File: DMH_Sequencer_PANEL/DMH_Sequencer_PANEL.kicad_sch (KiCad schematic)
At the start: 53 parts, among them J0 Panel_GND_Solder_Wire_Pad

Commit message: Main controls position test ongoing
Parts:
- added H1: LED Step 1, SynthStuff:MountingHole_LED_3mm_R, symbol Mechanical:MountingHole
- added H1003, H1004, H1007, H1008: MountingHole_Rails, SynthStuff:MountingHole_Rails, symbol SynthStuff:MountingHole_Rails
- added H2: LED Step 2, SynthStuff:MountingHole_LED_3mm_R, symbol Mechanical:MountingHole
- added H3: LED Step 3, SynthStuff:MountingHole_LED_3mm_R, symbol Mechanical:MountingHole
- added H33: LED Step 9, SynthStuff:MountingHole_LED_3mm_R, symbol Mechanical:MountingHole
- added H34: LED Step 10, SynthStuff:MountingHole_LED_3mm_R, symbol Mechanical:MountingHole
- added H35: LED Step 11, SynthStuff:MountingHole_LED_3mm_R, symbol Mechanical:MountingHole
- added H36: LED Step 12, SynthStuff:MountingHole_LED_3mm_R, symbol Mechanical:MountingHole
- added H37: LED Step 13, SynthStuff:MountingHole_LED_3mm_R, symbol Mechanical:MountingHole
- added H38: LED Step 14, SynthStuff:MountingHole_LED_3mm_R, symbol Mechanical:MountingHole
- added H39: LED Step 15, SynthStuff:MountingHole_LED_3mm_R, symbol Mechanical:MountingHole
- added H4: LED Step 4, SynthStuff:MountingHole_LED_3mm_R, symbol Mechanical:MountingHole
- added H40: LED Step 16, SynthStuff:MountingHole_LED_3mm_R, symbol Mechanical:MountingHole
- added H5: LED Step 5, SynthStuff:MountingHole_LED_3mm_R, symbol Mechanical:MountingHole
- added H6: LED Step 6, SynthStuff:MountingHole_LED_3mm_R, symbol Mechanical:MountingHole
- added H65: Gate Out 1, SynthStuff:Jack_6.35mm_Cutout_Output_v6, symbol SynthStuff:MountingHole_Jack6.35mm_Output_v2
- added H66: Gate Out 2, SynthStuff:Jack_6.35mm_Cutout_Output_v6, symbol SynthStuff:MountingHole_Jack6.35mm_Output_v2
- added H67: Gate Out 3, SynthStuff:Jack_6.35mm_Cutout_Output_v6, symbol SynthStuff:MountingHole_Jack6.35mm_Output_v2
- added H68: Gate Out 4, SynthStuff:Jack_6.35mm_Cutout_Output_v6, symbol SynthStuff:MountingHole_Jack6.35mm_Output_v2
- added H69: Gate Out 5, SynthStuff:Jack_6.35mm_Cutout_Output_v6, symbol SynthStuff:MountingHole_Jack6.35mm_Output_v2
- added H7: LED Step 7, SynthStuff:MountingHole_LED_3mm_R, symbol Mechanical:MountingHole
- added H70: Gate Out 6, SynthStuff:Jack_6.35mm_Cutout_Output_v6, symbol SynthStuff:MountingHole_Jack6.35mm_Output_v2
- added H71: Gate Out 7, SynthStuff:Jack_6.35mm_Cutout_Output_v6, symbol SynthStuff:MountingHole_Jack6.35mm_Output_v2
- added H72: Gate Out 8, SynthStuff:Jack_6.35mm_Cutout_Output_v6, symbol SynthStuff:MountingHole_Jack6.35mm_Output_v2
- added H8: LED Step 8, SynthStuff:MountingHole_LED_3mm_R, symbol Mechanical:MountingHole
- H17: renamed from H13; value Gate Length 1 -> GL 1
- H18: renamed from H14; value Gate Length 2 -> GL 2
- H19: renamed from H15; value Gate Length 3 -> GL 3
- H20: renamed from H16; value Gate Length 4 -> GL 4
- H21: renamed from H17; value Gate Length 5 -> GL 5
- H22: renamed from H18; value Gate Length 6 -> GL 6
- H23: renamed from H19; value Gate Length 7 -> GL 7
- H24: renamed from H20; value Gate Length 8 -> GL 8
- H49: renamed from H29; value Gate Length 9 -> GL 9
- H50: renamed from H30; value Gate Length 10 -> GL 10
- H51: renamed from H31; value Gate Length 11 -> GL 11
- H52: renamed from H32; value Gate Length 12 -> GL 12
- H53: renamed from H33; value Gate Length 13 -> GL 13
- H54: renamed from H34; value Gate Length 14 -> GL 14
- H55: renamed from H35; value Gate Length 15 -> GL 15
- H56: renamed from H36; value Gate Length 16 -> GL 16
- renumbered H6 to H10, H1 to H1001, H2 to H1002, H3 to H1005, H4 to H1006, H7 to H11, H8 to H12, H9 to H13, H10 to H14, H11 to H15, H12 to H16, H37 to H25, H38 to H26, H39 to H27, H40 to H28, H41 to H29, H42 to H30, H43 to H31, H44 to H32, H21 to H41, H22 to H42, H23 to H43, H24 to H44, H25 to H45, H26 to H46, H27 to H47, H28 to H48, H45 to H57, H46 to H58, H47 to H59, H48 to H60, H49 to H61, H50 to H62, H51 to H63, H52 to H64, H5 to H9
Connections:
- net GND: now also H1003.1, H1004.1, H1007.1, H1008.1
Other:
- moved on the sheet: H10, H1002, H1006, H11, H12, H13, H14, H15, H16, H17, H18, H19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

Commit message: First Layout ready
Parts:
- added H73: Clock, SynthStuff:Pot_Cutout_Medium_v2, symbol SynthStuff:MountingHole_Pot
- added H74: Clk CV Amt, SynthStuff:Pot_Cutout_Tiny_attv_P110KH1, symbol SynthStuff:MountingHole_Pot
- added H75: Transp, SynthStuff:Pot_Cutout_Tiny, symbol SynthStuff:MountingHole_Pot
- added H76: Transp CV Amt, SynthStuff:Pot_Cutout_Tiny_attv_P110KH1, symbol SynthStuff:MountingHole_Pot
- added H77: Slew, SynthStuff:Pot_Cutout_Tiny, symbol SynthStuff:MountingHole_Pot
- added H78: Slew CV Amt, SynthStuff:Pot_Cutout_Tiny_attv_P110KH1, symbol SynthStuff:MountingHole_Pot
- added H79: Direction, SynthStuff:Selector_Cutout_5pos, symbol SynthStuff:MountingHole_Pot
- added H80: Mode, SynthStuff:Toggle_Switch_TE_Cutout, symbol SynthStuff:MountingHole_ToggleSwitch
- added H81: Clock, SynthStuff:Toggle_Switch_TE_Cutout, symbol SynthStuff:MountingHole_ToggleSwitch
- added H82: Quant, SynthStuff:Toggle_Switch_TE_Cutout, symbol SynthStuff:MountingHole_ToggleSwitch
- added H83: Step, SynthStuff:MX_switch_Cutout, symbol Mechanical:MountingHole
- added H84: Reset, SynthStuff:MX_switch_Cutout, symbol Mechanical:MountingHole
- added H85: LED Quant, SynthStuff:MountingHole_LED_3mm_R, symbol Mechanical:MountingHole
- added H86: CV 1-8, SynthStuff:Jack_6.35mm_Cutout_Output_v6, symbol SynthStuff:MountingHole_Jack6.35mm_Output_v2
- added H87: CV 9-16, SynthStuff:Jack_6.35mm_Cutout_Output_v6, symbol SynthStuff:MountingHole_Jack6.35mm_Output_v2
- added H88: Gate, SynthStuff:Jack_6.35mm_Cutout_Output_v6, symbol SynthStuff:MountingHole_Jack6.35mm_Output_v2
- added H89: Gate 9-16, SynthStuff:Jack_6.35mm_Cutout_Output_v6, symbol SynthStuff:MountingHole_Jack6.35mm_Output_v2
- added H90: Clock, SynthStuff:Jack_6.35mm_Cutout_v3, symbol SynthStuff:MountingHole_Jack6.35mm_v2
- added H91: Reset, SynthStuff:Jack_6.35mm_Cutout_v3, symbol SynthStuff:MountingHole_Jack6.35mm_v2
- added H92: Transp, SynthStuff:Jack_6.35mm_Cutout_v3, symbol SynthStuff:MountingHole_Jack6.35mm_v2
- H65, H66, H67, H68, H69, H70, H71, H72: now not fitted

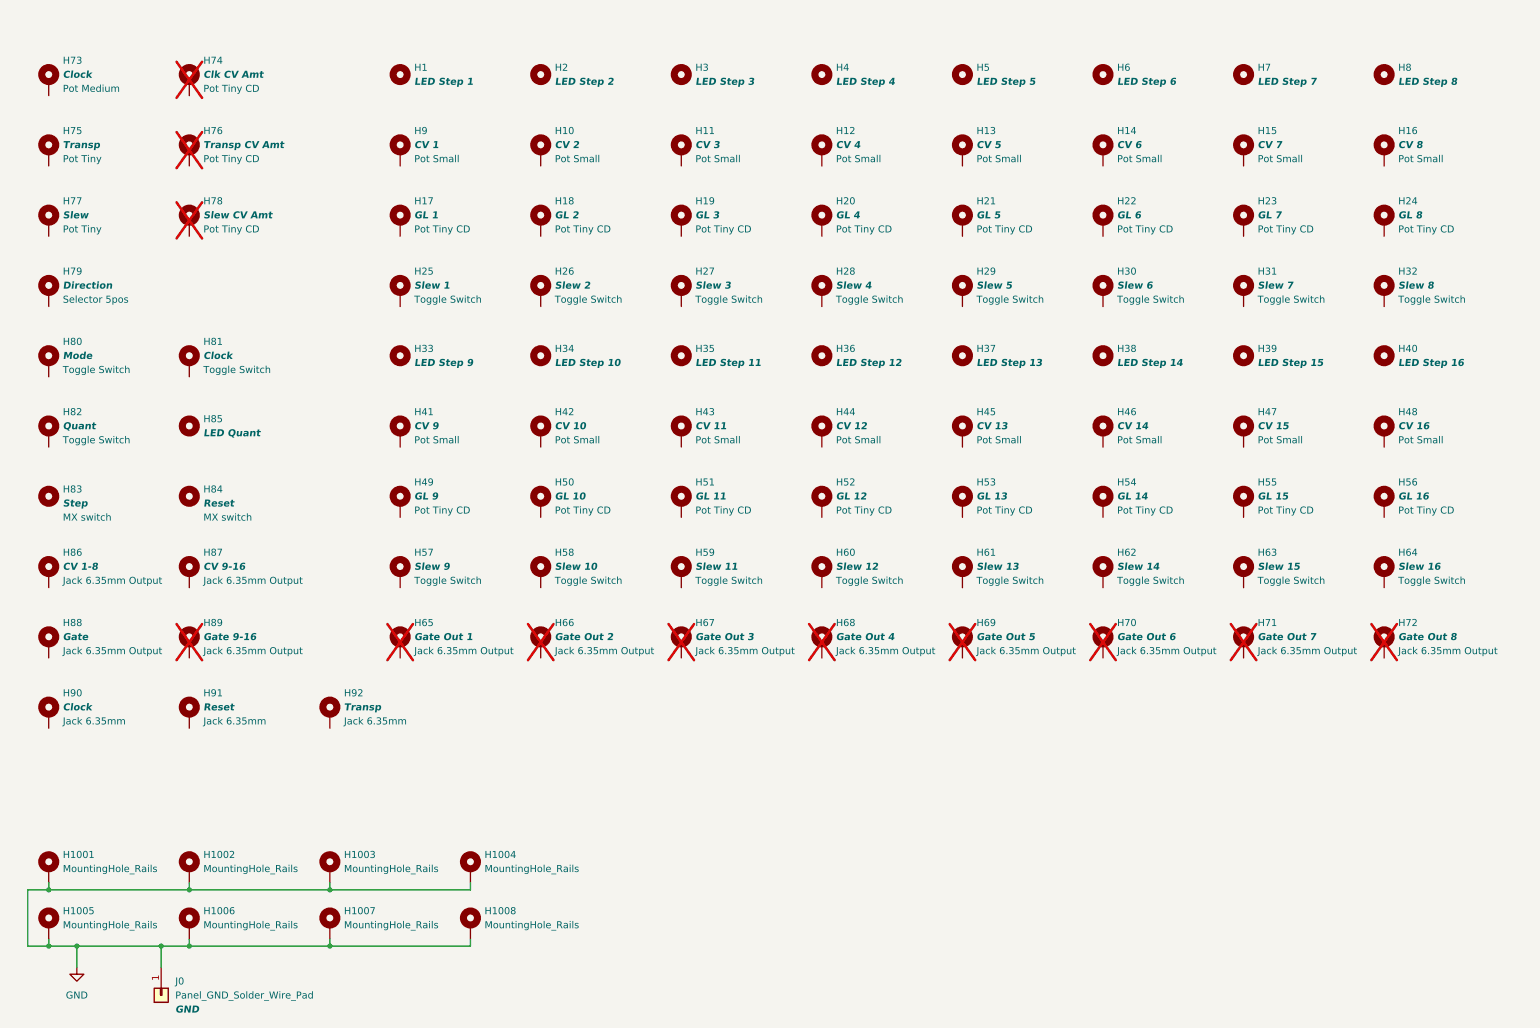
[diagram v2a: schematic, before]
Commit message: Updated selector 3D model
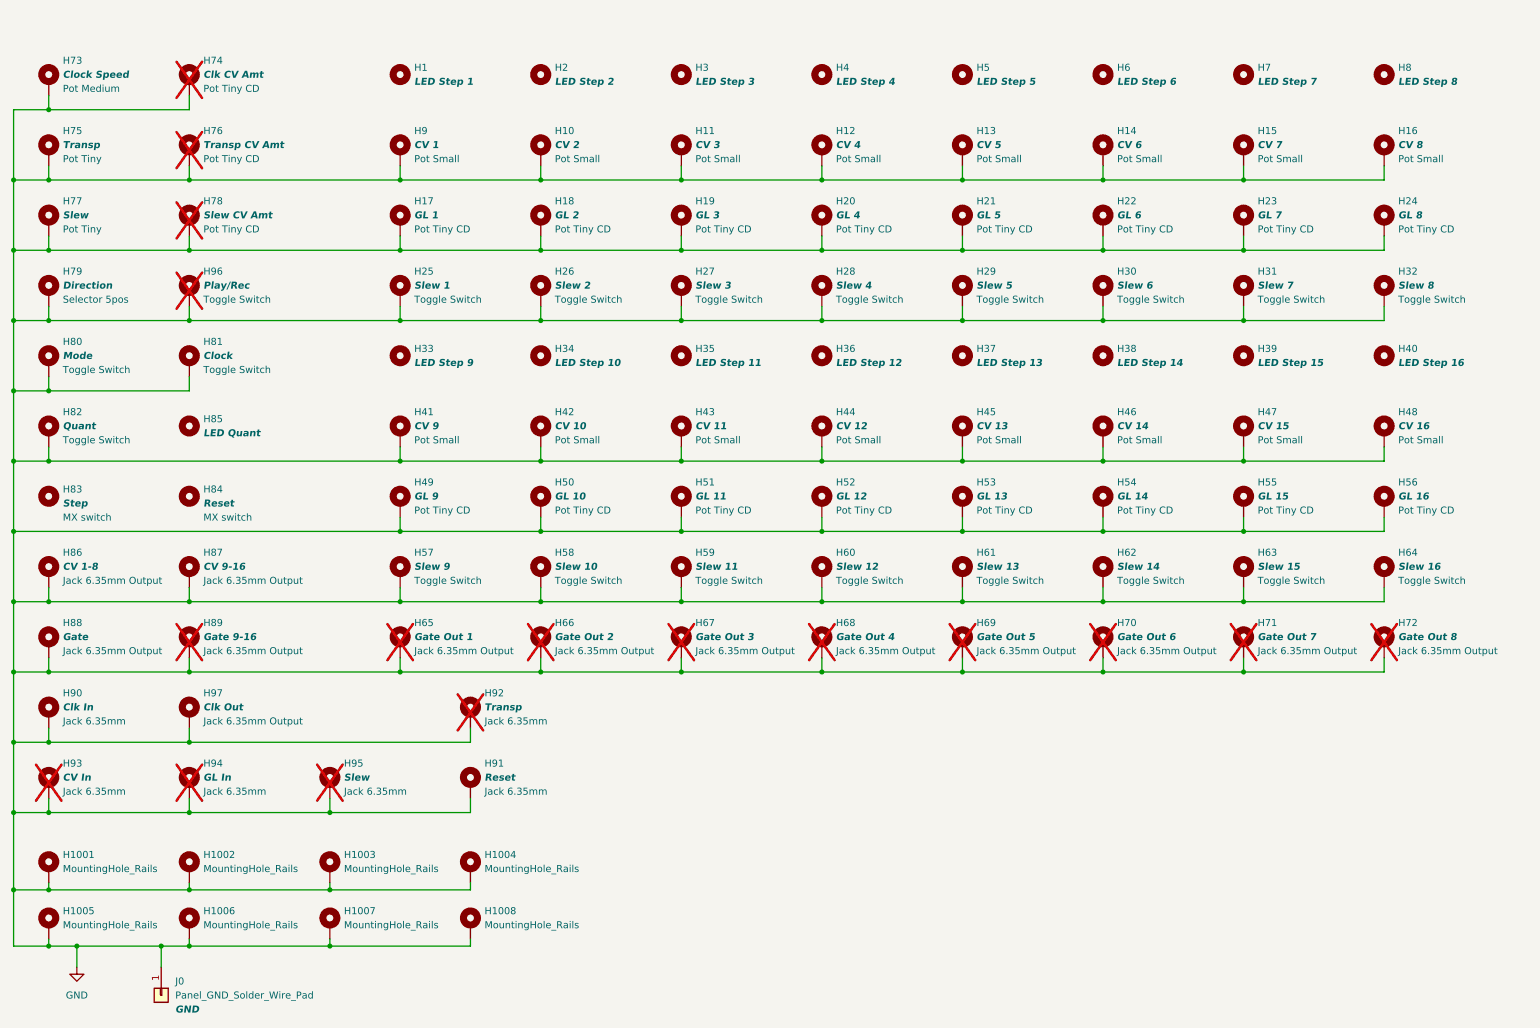
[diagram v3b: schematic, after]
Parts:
- added H93: CV In, SynthStuff:Jack_6.35mm_Cutout_v3, symbol SynthStuff:MountingHole_Jack6.35mm_v2
- added H94: GL In, SynthStuff:Jack_6.35mm_Cutout_v3, symbol SynthStuff:MountingHole_Jack6.35mm_v2
- added H95: Slew, SynthStuff:Jack_6.35mm_Cutout_v3, symbol SynthStuff:MountingHole_Jack6.35mm_v2
- added H96: Play/Rec, SynthStuff:Toggle_Switch_TE_Cutout, symbol SynthStuff:MountingHole_ToggleSwitch
- added H97: Clk Out, SynthStuff:Jack_6.35mm_Cutout_Output_v6, symbol SynthStuff:MountingHole_Jack6.35mm_Output_v2
- H73: value Clock -> Clock Speed
- H85: footprint SynthStuff:MountingHole_LED_3mm_R -> SynthStuff:MountingHole_LED_3mm_B
- H90: value Clock -> Clk In
- H92: now not fitted
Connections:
- net GND: now also H10.1, H11.1, H12.1, H13.1, H14.1, H15.1, H16.1, H17.1, H18.1, H19.1, H20.1, H21.1, H22.1, H23.1, H24.1, H25.1, H26.1, H27.1, H28.1, H29.1, H30.1, H31.1, H32.1, H41.1, H42.1, H43.1, H44.1, H45.1, H46.1, H47.1, H48.1, H49.1, H50.1, H51.1, H52.1, H53.1, H54.1, H55.1, H56.1, H57.1, H58.1, H59.1, H60.1, H61.1, H62.1, H63.1, H64.1, H65.1, H66.1, H67.1, H68.1, H69.1, H70.1, H71.1, H72.1, H73.1, H74.1, H75.1, H76.1, H77.1, H78.1, H79.1, H80.1, H81.1, H82.1, H86.1, H87.1, H88.1, H89.1, H9.1, H90.1, H91.1, H92.1, H93.1, H94.1, H95.1, H96.1, H97.1
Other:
- moved on the sheet: H91

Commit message: Added clock PPQN selector
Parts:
- added H98: LED Clock, SynthStuff:MountingHole_LED_3mm_R, symbol Mechanical:MountingHole
- added H99: Clk PPQN, SynthStuff:Selector_Cutout_SRBV151102, symbol SynthStuff:MountingHole_Selector
- H75: footprint SynthStuff:Pot_Cutout_Tiny -> SynthStuff:Pot_Cutout_Tiny_attv_RD901F
- H79: footprint SynthStuff:Selector_Cutout_5pos -> SynthStuff:Selector_Cutout_SRBV151102; symbol SynthStuff:MountingHole_Pot -> SynthStuff:MountingHole_Selector
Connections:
- net GND: now also H99.1

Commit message: jack placemente ongoig
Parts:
- added H100: Gate 1, SynthStuff:Jack_6.35mm_Cutout_Output_v6, symbol SynthStuff:MountingHole_Jack6.35mm_Output_v2
- added H101: Gate 2, SynthStuff:Jack_6.35mm_Cutout_Output_v6, symbol SynthStuff:MountingHole_Jack6.35mm_Output_v2
- added H102: Gate 3, SynthStuff:Jack_6.35mm_Cutout_Output_v6, symbol SynthStuff:MountingHole_Jack6.35mm_Output_v2
- added H103: Gate 4, SynthStuff:Jack_6.35mm_Cutout_Output_v6, symbol SynthStuff:MountingHole_Jack6.35mm_Output_v2
- added H104: Gate 5, SynthStuff:Jack_6.35mm_Cutout_Output_v6, symbol SynthStuff:MountingHole_Jack6.35mm_Output_v2
- added H105: Gate 6, SynthStuff:Jack_6.35mm_Cutout_Output_v6, symbol SynthStuff:MountingHole_Jack6.35mm_Output_v2
- added H106: Gate 7, SynthStuff:Jack_6.35mm_Cutout_Output_v6, symbol SynthStuff:MountingHole_Jack6.35mm_Output_v2
- added H107: Gate 8, SynthStuff:Jack_6.35mm_Cutout_Output_v6, symbol SynthStuff:MountingHole_Jack6.35mm_Output_v2
- added H108: Gate 9, SynthStuff:Jack_6.35mm_Cutout_Output_v6, symbol SynthStuff:MountingHole_Jack6.35mm_Output_v2
- added H109: Gate 10, SynthStuff:Jack_6.35mm_Cutout_Output_v6, symbol SynthStuff:MountingHole_Jack6.35mm_Output_v2
- added H110: Gate 11, SynthStuff:Jack_6.35mm_Cutout_Output_v6, symbol SynthStuff:MountingHole_Jack6.35mm_Output_v2
- added H111: Gate 12, SynthStuff:Jack_6.35mm_Cutout_Output_v6, symbol SynthStuff:MountingHole_Jack6.35mm_Output_v2
- added H112: Gate 13, SynthStuff:Jack_6.35mm_Cutout_Output_v6, symbol SynthStuff:MountingHole_Jack6.35mm_Output_v2
- added H113: Gate 14, SynthStuff:Jack_6.35mm_Cutout_Output_v6, symbol SynthStuff:MountingHole_Jack6.35mm_Output_v2
- added H114: Gate 15, SynthStuff:Jack_6.35mm_Cutout_Output_v6, symbol SynthStuff:MountingHole_Jack6.35mm_Output_v2
- added H115: Gate 16, SynthStuff:Jack_6.35mm_Cutout_Output_v6, symbol SynthStuff:MountingHole_Jack6.35mm_Output_v2
- H65: value Gate Out 1 -> Gate 1
- H66: value Gate Out 2 -> Gate 2
- H67: value Gate Out 3 -> Gate 3
- H68: value Gate Out 4 -> Gate 4
- H69: value Gate Out 5 -> Gate 5
- H70: value Gate Out 6 -> Gate 6
- H71: value Gate Out 7 -> Gate 7
- H72: value Gate Out 8 -> Gate 8
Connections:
- net GND: now also H100.1, H101.1, H102.1, H103.1, H104.1, H105.1, H106.1, H107.1, H108.1, H109.1, H110.1, H111.1, H112.1, H113.1, H114.1, H115.1

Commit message: Redistributed glide switches and gate outs
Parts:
- H100, H65: value Gate 1 -> 1
- H101, H66: value Gate 2 -> 2
- H102, H67: value Gate 3 -> 3
- H103, H68: value Gate 4 -> 4
- H104, H69: value Gate 5 -> 5
- H105, H70: value Gate 6 -> 6
- H106, H71: value Gate 7 -> 7
- H107, H72: value Gate 8 -> 8
- H108: value Gate 9 -> 9
- H109: value Gate 10 -> 10
- H110: value Gate 11 -> 11
- H111: value Gate 12 -> 12
- H112: value Gate 13 -> 13
- H113: value Gate 14 -> 14
- H114: value Gate 15 -> 15
- H115: value Gate 16 -> 16
- H25: value Slew 1 -> 1
- H26: value Slew 2 -> 2
- H27: value Slew 3 -> 3
- H28: value Slew 4 -> 4
- H29: value Slew 5 -> 5
- H30: value Slew 6 -> 6
- H31: value Slew 7 -> 7
- H32: value Slew 8 -> 8
- H57: value Slew 9 -> 9
- H58: value Slew 10 -> 10
- H59: value Slew 11 -> 11
- H60: value Slew 12 -> 12
- H61: value Slew 13 -> 13
- H62: value Slew 14 -> 14
- H63: value Slew 15 -> 15
- H64: value Slew 16 -> 16
- H77: value Slew -> Glide
- H78: value Slew CV Amt -> CV Amt
- H89: value Gate 9-16 -> 9-16
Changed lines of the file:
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@@
 			)
 		)
-		(property "Value" "Slew"
+		(property "Value" "Glide"
 			(at 27.94 50.8 0)
 			(effects
@@
 			)
 		)
-		(property "Value" "Slew 3"
+		(property "Value" "3"
 			(at 142.24 63.5 0)
 			(effects
@@
 			)
 		)
-		(property "Value" "Slew 13"
+		(property "Value" "13"
 			(at 193.04 114.3 0)
 			(effects
@@
 			)
 		)
-		(property "Value" "Gate 13"
+		(property "Value" "13"
 			(at 228.6 153.924 90)
 			(effects
@@
 			)
 		)
-		(property "Value" "Gate 1"
+		(property "Value" "1"
 			(at 177.8 138.684 90)
 			(effects
@@
 			)
 		)
-		(property "Value" "Slew 14"
+		(property "Value" "14"
 			(at 218.44 114.3 0)
 			(effects
@@
 			)
 		)
-		(property "Value" "Gate 6"
+		(property "Value" "6"
 			(at 218.44 127 90)
 			(effects
@@
 			)
 		)
-		(property "Value" "Gate 10"
+		(property "Value" "10"
 			(at 190.5 153.924 90)
 			(effects
@@
 			)
 		)
-		(property "Value" "Slew 16"
+		(property "Value" "16"
 			(at 269.24 114.3 0)
 			(effects
@@
 			)
 		)
-		(property "Value" "Gate 8"
+		(property "Value" "8"
 			(at 266.7 138.684 90)
 			(effects
@@
 			)
 		)
-		(property "Value" "Gate 9-16"
+		(property "Value" "9-16"
 			(at 53.34 127 90)
 			(effects
@@
 			)
 		)
-		(property "Value" "Gate 8"
+		(property "Value" "8"
 			(at 269.24 127 90)
 			(effects
@@
 			)
 		)
-		(property "Value" "Slew 6"
+		(property "Value" "6"
 			(at 218.44 63.5 0)
 			(effects
@@
 			)
 		)
-		(property "Value" "Slew 1"
+		(property "Value" "1"
 			(at 91.44 63.5 0)
 			(effects
@@
 			)
 		)
-		(property "Value" "Gate 7"
+		(property "Value" "7"
 			(at 243.84 127 90)
 			(effects
@@
 			)
 		)
-		(property "Value" "Slew 7"
+		(property "Value" "7"
 			(at 243.84 63.5 0)
 			(effects
@@
 			)
 		)
-		(property "Value" "Gate 9"
+		(property "Value" "9"
 			(at 177.8 153.924 90)
 			(effects
@@
 			)
 		)
-		(property "Value" "Gate 11"
+		(property "Value" "11"
 			(at 203.2 153.924 90)
 			(effects
@@
 			)
 		)
-		(property "Value" "Slew CV Amt"
+		(property "Value" "CV Amt"
 			(at 53.34 50.8 0)
 			(effects
@@
 			)
 		)
-		(property "Value" "Slew 10"
+		(property "Value" "10"
 			(at 116.84 114.3 0)
 			(effects
@@
 			)
 		)
-		(property "Value" "Gate 5"
+		(property "Value" "5"
 			(at 193.04 127 90)
 			(effects
@@
 			)
 		)
-		(property "Value" "Gate 4"
+		(property "Value" "4"
 			(at 167.64 127 90)
 			(effects
@@
 			)
 		)
-		(property "Value" "Slew 8"
+		(property "Value" "8"
 			(at 269.24 63.5 0)
 			(effects
@@
 			)
 		)
-		(property "Value" "Gate 3"
+		(property "Value" "3"
 			(at 142.24 127 90)
 			(effects
@@
 			)
 		)
-		(property "Value" "Gate 3"
+		(property "Value" "3"
 			(at 203.2 138.684 90)
 			(effects
@@
 			)
 		)
-		(property "Value" "Gate 1"
+		(property "Value" "1"
 			(at 91.44 127 90)
 			(effects
@@
 			)
 		)
-		(property "Value" "Slew 12"
+		(property "Value" "12"
 			(at 167.64 114.3 0)
 			(effects
@@
 			)
 		)
-		(property "Value" "Slew 5"
+		(property "Value" "5"
 			(at 193.04 63.5 0)
 			(effects
@@
 			)
 		)
-		(property "Value" "Slew 15"
+		(property "Value" "15"
 			(at 243.84 114.3 0)
 			(effects
@@
 			)
 		)
-		(property "Value" "Gate 2"
+		(property "Value" "2"
 			(at 116.84 127 90)
 			(effects
@@
 			)
 		)
-		(property "Value" "Gate 15"
+		(property "Value" "15"
 			(at 254 153.924 90)
 			(effects
@@
 			)
 		)
-		(property "Value" "Slew 11"
+		(property "Value" "11"
 			(at 142.24 114.3 0)
 			(effects
@@
 			)
 		)
-		(property "Value" "Gate 6"
+		(property "Value" "6"
 			(at 241.3 138.684 90)
 			(effects
@@
 			)
 		)
-		(property "Value" "Gate 2"
+		(property "Value" "2"
 			(at 190.5 138.684 90)
 			(effects
@@
 			)
 		)
-		(property "Value" "Gate 14"
+		(property "Value" "14"
 			(at 241.3 153.924 90)
 			(effects
@@
 			)
 		)
-		(property "Value" "Gate 7"
+		(property "Value" "7"
 			(at 254 138.684 90)
 			(effects
@@
 			)
 		)
-		(property "Value" "Gate 16"
+		(property "Value" "16"
 			(at 266.7 153.924 90)
 			(effects
@@
 			)
 		)
-		(property "Value" "Gate 4"
+		(property "Value" "4"
 			(at 215.9 138.684 90)
 			(effects
@@
 			)
 		)
-		(property "Value" "Gate 5"
+		(property "Value" "5"
 			(at 228.6 138.684 90)
 			(effects
@@
 			)
 		)
-		(property "Value" "Gate 12"
+		(property "Value" "12"
 			(at 215.9 153.924 90)
 			(effects
@@
 			)
 		)
-		(property "Value" "Slew 4"
+		(property "Value" "4"
 			(at 167.64 63.5 0)
 			(effects
@@
 			)
 		)
-		(property "Value" "Slew 9"
+		(property "Value" "9"
 			(at 91.44 114.3 0)
 			(effects
@@
 			)
 		)
-		(property "Value" "Slew 2"
+		(property "Value" "2"
 			(at 116.84 63.5 0)
 			(effects

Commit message: Added range selection switch
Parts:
- H77: value Glide -> Slew
- H80: value Mode -> Range
- H82: value Quant -> 8 / 16
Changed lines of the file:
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@@
 			)
 		)
-		(property "Value" "Glide"
+		(property "Value" "Slew"
 			(at 27.94 50.8 0)
 			(effects
@@
 			)
 		)
-		(property "Value" "Quant"
+		(property "Value" "8 / 16"
 			(at 27.94 88.9 0)
 			(effects
@@
 			)
 		)
-		(property "Value" "Mode"
+		(property "Value" "Range"
 			(at 27.94 76.2 0)
 			(effects
